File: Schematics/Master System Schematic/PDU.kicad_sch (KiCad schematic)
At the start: 0 parts

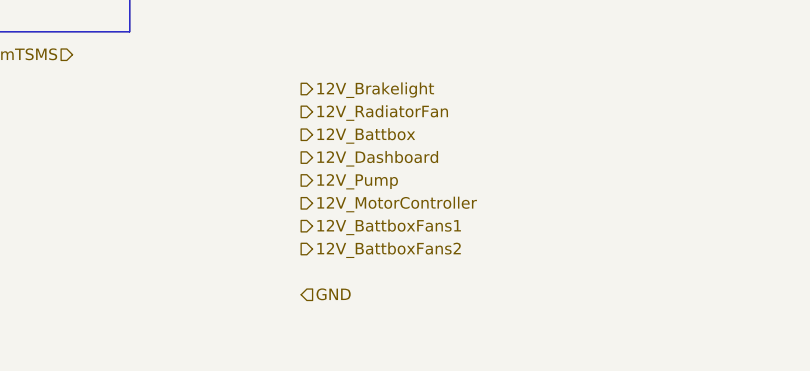
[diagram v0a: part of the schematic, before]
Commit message: Added battbox fans
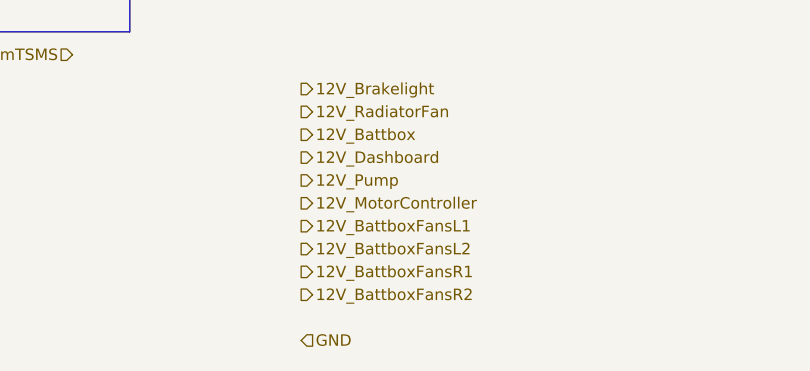
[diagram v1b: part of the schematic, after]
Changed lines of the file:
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@@
     (effects (font (size 3.9878 3.9878)) (justify left bottom))
   )
-  (hierarchical_label "GND" (shape input) (at 157.48 129.54 0)
+  (hierarchical_label "GND" (shape input) (at 157.48 134.62 0)
     (effects (font (size 1.27 1.27)) (justify left))
   )
@@
     (effects (font (size 1.27 1.27)) (justify right))
   )
-  (hierarchical_label "12V_BattboxFans2" (shape output) (at 157.48 124.46 0)
+  (hierarchical_label "12V_BattboxFansL2" (shape output) (at 157.48 124.46 0)
+    (effects (font (size 1.27 1.27)) (justify left))
+  )
+  (hierarchical_label "12V_BattboxFansR1" (shape output) (at 157.48 127 0)
     (effects (font (size 1.27 1.27)) (justify left))
   )
@@
     (effects (font (size 1.27 1.27)) (justify right))
   )
-  (hierarchical_label "12V_BattboxFans1" (shape output) (at 157.48 121.92 0)
+  (hierarchical_label "12V_BattboxFansL1" (shape output) (at 157.48 121.92 0)
     (effects (font (size 1.27 1.27)) (justify left))
   )
@@
     (effects (font (size 1.27 1.27)) (justify left))
   )
+  (hierarchical_label "12V_BattboxFansR2" (shape output) (at 157.48 129.54 0)
+    (effects (font (size 1.27 1.27)) (justify left))
+  )

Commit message: IDrk
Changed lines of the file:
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@@
     (effects (font (size 3.9878 3.9878)) (justify left bottom))
   )
-  (hierarchical_label "GND" (shape input) (at 157.48 134.62 0)
+  (hierarchical_label "CAN_S" (shape passive) (at 157.48 146.05 0)
+    (effects (font (size 1.27 1.27)) (justify left))
+  )
+  (hierarchical_label "CAN_L" (shape bidirectional) (at 157.48 140.97 0)
+    (effects (font (size 1.27 1.27)) (justify left))
+  )
+  (hierarchical_label "GND" (shape passive) (at 157.48 134.62 0)
     (effects (font (size 1.27 1.27)) (justify left))
   )
@@
     (effects (font (size 1.27 1.27)) (justify left))
   )
+  (hierarchical_label "CAN_H" (shape bidirectional) (at 157.48 143.51 0)
+    (effects (font (size 1.27 1.27)) (justify left))
+  )

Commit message: Initial LV 2023 Competition Update
List of questions/comments: https://docs.google.com/document/d/1Jezx0FskMhwUdHdk8isXV7eDmPDUZPOb6vodgO5P4QI/edit?usp=sharing
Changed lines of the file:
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@@
     (effects (font (size 3.9878 3.9878)) (justify left bottom))
   )
-  (hierarchical_label "CAN_S" (shape passive) (at 157.48 146.05 0)
+  (hierarchical_label "12V_GLVMS2" (shape input) (at 133.35 66.04 180)
+    (effects (font (size 1.27 1.27)) (justify right))
+  )
+  (hierarchical_label "GND_BattboxFansR2" (shape input) (at 157.48 139.7 0)
     (effects (font (size 1.27 1.27)) (justify left))
   )
-  (hierarchical_label "CAN_L" (shape bidirectional) (at 157.48 140.97 0)
+  (hierarchical_label "CAN_S" (shape passive) (at 157.48 156.21 0)
     (effects (font (size 1.27 1.27)) (justify left))
   )
-  (hierarchical_label "GND" (shape passive) (at 157.48 134.62 0)
+  (hierarchical_label "CAN_L" (shape bidirectional) (at 157.48 151.13 0)
+    (effects (font (size 1.27 1.27)) (justify left))
+  )
+  (hierarchical_label "GND_BattboxFansL2" (shape input) (at 157.48 134.62 0)
     (effects (font (size 1.27 1.27)) (justify left))
   )
@@
     (effects (font (size 1.27 1.27)) (justify right))
   )
-  (hierarchical_label "SD_FromBRBs" (shape input) (at 132.08 77.47 180)
+  (hierarchical_label "SD_From_Side_BRBs" (shape input) (at 133.35 73.66 180)
     (effects (font (size 1.27 1.27)) (justify right))
   )
@@
     (effects (font (size 1.27 1.27)) (justify right))
   )
-  (hierarchical_label "SD_FromTSMS" (shape input) (at 132.08 102.87 180)
+  (hierarchical_label "SD_FromTSMS" (shape input) (at 133.35 78.74 180)
     (effects (font (size 1.27 1.27)) (justify right))
   )
@@
     (effects (font (size 1.27 1.27)) (justify left))
   )
-  (hierarchical_label "SD_ToBRBs" (shape output) (at 132.08 74.93 180)
+  (hierarchical_label "SD_To_Side_BRBs" (shape output) (at 133.35 71.12 180)
     (effects (font (size 1.27 1.27)) (justify right))
   )
-  (hierarchical_label "SD_ToBrakeOT" (shape output) (at 132.08 80.01 180)
+  (hierarchical_label "SD_ToBrakeOT" (shape output) (at 133.35 76.2 180)
     (effects (font (size 1.27 1.27)) (justify right))
   )
@@
     (effects (font (size 1.27 1.27)) (justify right))
   )
-  (hierarchical_label "12V_Breaker" (shape input) (at 132.08 72.39 180)
+  (hierarchical_label "12V_GLVMS1" (shape input) (at 133.35 68.58 180)
     (effects (font (size 1.27 1.27)) (justify right))
   )
@@
   (hierarchical_label "IMD_Fault_Indicator" (shape output) (at 82.55 97.79 180)
     (effects (font (size 1.27 1.27)) (justify right))
+  )
+  (hierarchical_label "GND_BattboxFansR1" (shape input) (at 157.48 137.16 0)
+    (effects (font (size 1.27 1.27)) (justify left))
   )
   (hierarchical_label "SD_ToCockpit" (shape output) (at 132.08 91.44 180)
@@
     (effects (font (size 1.27 1.27)) (justify left))
   )
+  (hierarchical_label "GND_BattboxFansL1" (shape input) (at 157.48 132.08 0)
+    (effects (font (size 1.27 1.27)) (justify left))
+  )
   (hierarchical_label "12V_BattboxFansR2" (shape output) (at 157.48 129.54 0)
     (effects (font (size 1.27 1.27)) (justify left))
@@
     (effects (font (size 1.27 1.27)) (justify right))
   )
+  (hierarchical_label "12V_GLVMS3" (shape input) (at 133.35 63.5 180)
+    (effects (font (size 1.27 1.27)) (justify right))
+  )
   (hierarchical_label "12V_Dashboard" (shape output) (at 157.48 114.3 0)
     (effects (font (size 1.27 1.27)) (justify left))
   )
-  (hierarchical_label "CAN_H" (shape bidirectional) (at 157.48 143.51 0)
+  (hierarchical_label "CAN_H" (shape bidirectional) (at 157.48 153.67 0)
     (effects (font (size 1.27 1.27)) (justify left))
   )

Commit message: Addressed review feedback
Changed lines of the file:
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@@
     (comment 2 "For authors and other info, contact Chief Electrical Engineer")
   )
+  (junction (at 138.43 66.04) (diameter 0) (color 0 0 0 0)
+  )
+  (junction (at 138.43 58.42) (diameter 0) (color 0 0 0 0)
+  )
+  (wire (pts (xy 152.4 151.13) (xy 152.4 153.67))
+    (stroke (width 0) (type default))
+  )
+  (wire (pts (xy 133.35 68.58) (xy 138.43 68.58))
+    (stroke (width 0) (type default))
+  )
+  (wire (pts (xy 138.43 58.42) (xy 138.43 60.96))
+    (stroke (width 0) (type default))
+  )
+  (wire (pts (xy 138.43 55.88) (xy 138.43 58.42))
+    (stroke (width 0) (type default))
+  )
   (polyline (pts (xy 59.69 100.33) (xy 138.43 100.33))
+    (stroke (width 0) (type default))
+  )
+  (wire (pts (xy 138.43 63.5) (xy 138.43 66.04))
+    (stroke (width 0) (type default))
+  )
+  (wire (pts (xy 133.35 55.88) (xy 138.43 55.88))
+    (stroke (width 0) (type default))
+  )
+  (wire (pts (xy 157.48 146.05) (xy 152.4 146.05))
+    (stroke (width 0) (type default))
+  )
+  (wire (pts (xy 152.4 158.75) (xy 157.48 158.75))
+    (stroke (width 0) (type default))
+  )
+  (wire (pts (xy 133.35 66.04) (xy 138.43 66.04))
+    (stroke (width 0) (type default))
+  )
+  (wire (pts (xy 152.4 148.59) (xy 157.48 148.59))
+    (stroke (width 0) (type default))
+  )
+  (wire (pts (xy 157.48 151.13) (xy 152.4 151.13))
+    (stroke (width 0) (type default))
+  )
+  (wire (pts (xy 138.43 60.96) (xy 133.35 60.96))
     (stroke (width 0) (type default))
   )
@@
     (stroke (width 0) (type default))
   )
+  (wire (pts (xy 152.4 153.67) (xy 157.48 153.67))
+    (stroke (width 0) (type default))
+  )
+  (wire (pts (xy 157.48 156.21) (xy 152.4 156.21))
+    (stroke (width 0) (type default))
+  )
+  (wire (pts (xy 152.4 146.05) (xy 152.4 148.59))
+    (stroke (width 0) (type default))
+  )
+  (wire (pts (xy 152.4 156.21) (xy 152.4 158.75))
+    (stroke (width 0) (type default))
+  )
+  (wire (pts (xy 133.35 63.5) (xy 138.43 63.5))
+    (stroke (width 0) (type default))
+  )
   (polyline (pts (xy 59.69 82.55) (xy 138.43 82.55))
     (stroke (width 0) (type default))
   )
+  (wire (pts (xy 138.43 66.04) (xy 138.43 68.58))
+    (stroke (width 0) (type default))
+  )
   (polyline (pts (xy 59.69 82.55) (xy 59.69 100.33))
+    (stroke (width 0) (type default))
+  )
+  (wire (pts (xy 133.35 58.42) (xy 138.43 58.42))
     (stroke (width 0) (type default))
   )
@@
     (effects (font (size 1.27 1.27)) (justify right))
   )
+  (hierarchical_label "Battery_GND1" (shape input) (at 133.35 60.96 180) (fields_autoplaced)
+    (effects (font (size 1.27 1.27)) (justify right))
+  )
   (hierarchical_label "GND_BattboxFansR2" (shape input) (at 157.48 139.7 0) (fields_autoplaced)
     (effects (font (size 1.27 1.27)) (justify left))
@@
     (effects (font (size 1.27 1.27)) (justify left))
   )
-  (hierarchical_label "CAN_L" (shape bidirectional) (at 157.48 151.13 0) (fields_autoplaced)
+  (hierarchical_label "Battery_GND2" (shape input) (at 133.35 58.42 180) (fields_autoplaced)
+    (effects (font (size 1.27 1.27)) (justify right))
+  )
+  (hierarchical_label "CAN_L" (shape bidirectional) (at 157.48 146.05 0) (fields_autoplaced)
     (effects (font (size 1.27 1.27)) (justify left))
   )
@@
     (effects (font (size 1.27 1.27)) (justify left))
   )
+  (hierarchical_label "CAN_S_Battery_Board" (shape passive) (at 157.48 158.75 0) (fields_autoplaced)
+    (effects (font (size 1.27 1.27)) (justify left))
+  )
   (hierarchical_label "IMD_Fault" (shape input) (at 82.55 95.25 180) (fields_autoplaced)
     (effects (font (size 1.27 1.27)) (justify right))
@@
   (hierarchical_label "BMS_Fault_Indicator" (shape output) (at 109.22 97.79 180) (fields_autoplaced)
     (effects (font (size 1.27 1.27)) (justify right))
+  )
+  (hierarchical_label "CAN_H" (shape bidirectional) (at 157.48 151.13 0) (fields_autoplaced)
+    (effects (font (size 1.27 1.27)) (justify left))
   )
   (hierarchical_label "IMD_Fault_Indicator" (shape output) (at 82.55 97.79 180) (fields_autoplaced)
@@
     (effects (font (size 1.27 1.27)) (justify right))
   )
+  (hierarchical_label "CAN_L_Battery_Board" (shape bidirectional) (at 157.48 148.59 0) (fields_autoplaced)
+    (effects (font (size 1.27 1.27)) (justify left))
+  )
   (hierarchical_label "12V_Brakelight" (shape output) (at 157.48 106.68 0) (fields_autoplaced)
     (effects (font (size 1.27 1.27)) (justify left))
@@
     (effects (font (size 1.27 1.27)) (justify left))
   )
+  (hierarchical_label "Battery_GND3" (shape input) (at 133.35 55.88 180) (fields_autoplaced)
+    (effects (font (size 1.27 1.27)) (justify right))
+  )
   (hierarchical_label "CAN_Fault" (shape input) (at 109.22 85.09 180) (fields_autoplaced)
     (effects (font (size 1.27 1.27)) (justify right))
@@
     (effects (font (size 1.27 1.27)) (justify left))
   )
-  (hierarchical_label "CAN_H" (shape bidirectional) (at 157.48 153.67 0) (fields_autoplaced)
+  (hierarchical_label "CAN_H_Battery_Board" (shape bidirectional) (at 157.48 153.67 0) (fields_autoplaced)
     (effects (font (size 1.27 1.27)) (justify left))
   )
